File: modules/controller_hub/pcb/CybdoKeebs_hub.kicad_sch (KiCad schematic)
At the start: 5 parts, among them J1 USB_C_Receptacle_USB2.0_14P, U1 RP2040, U2 CH334F

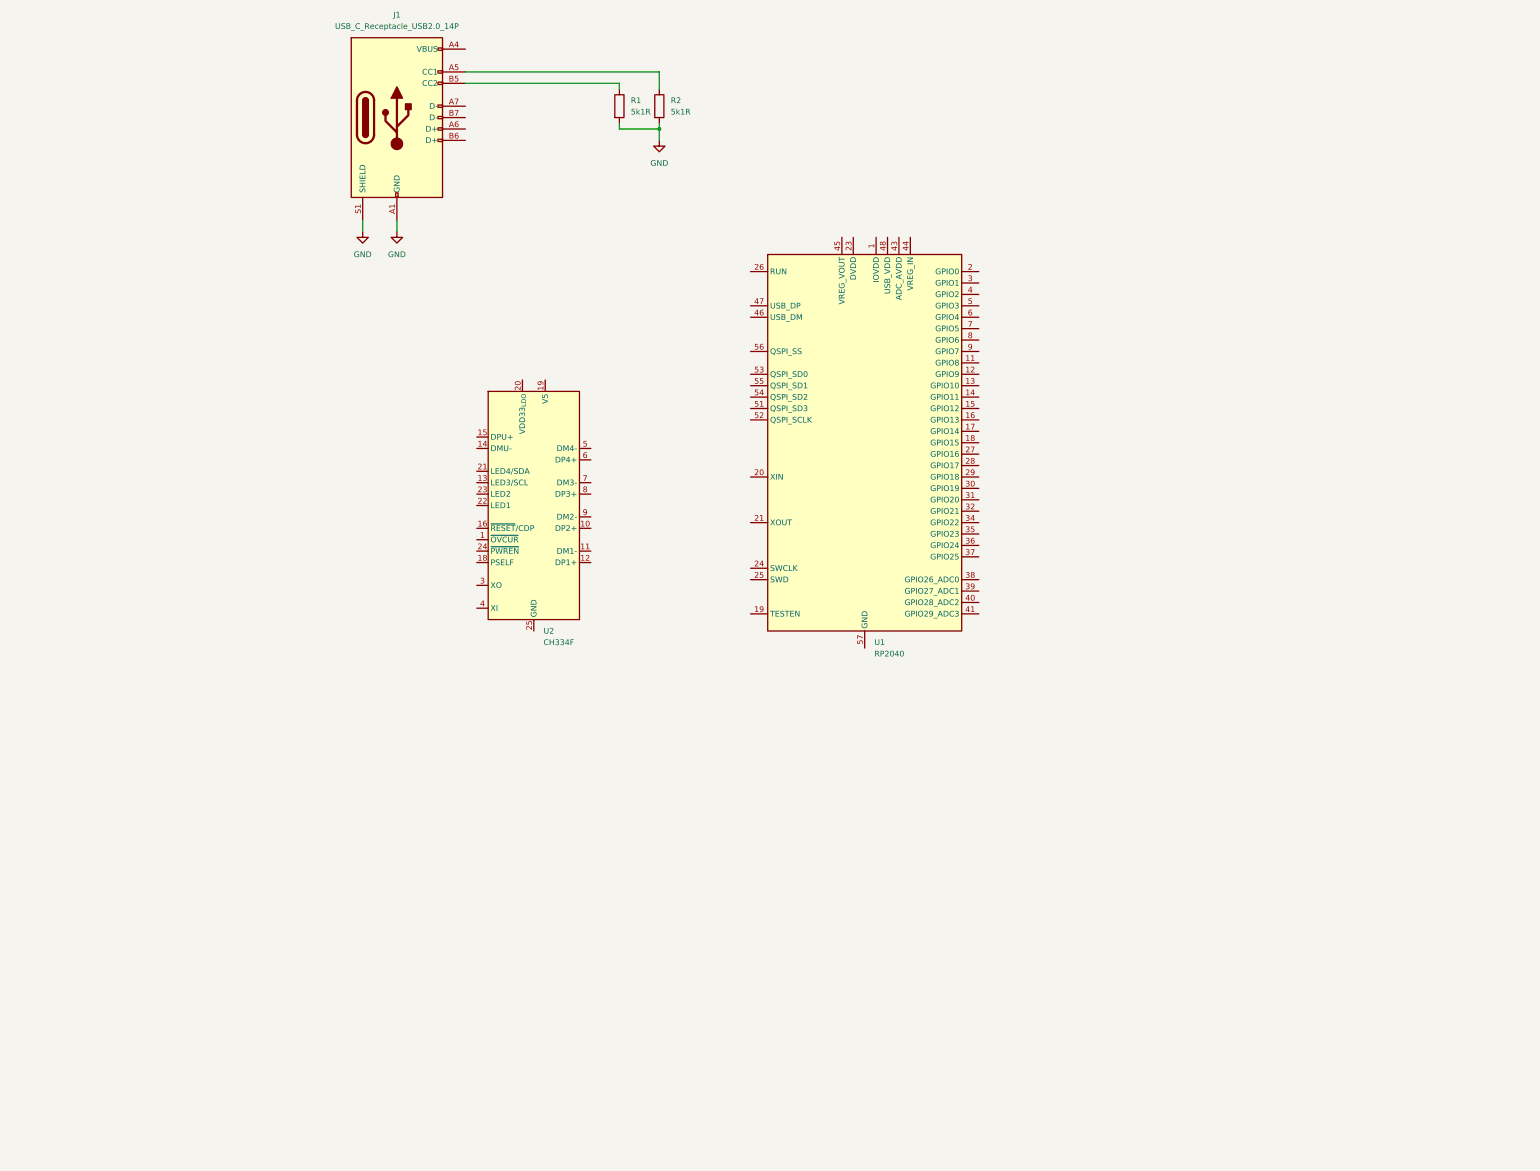
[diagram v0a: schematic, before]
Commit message: finish minimum system, add i2c connectors
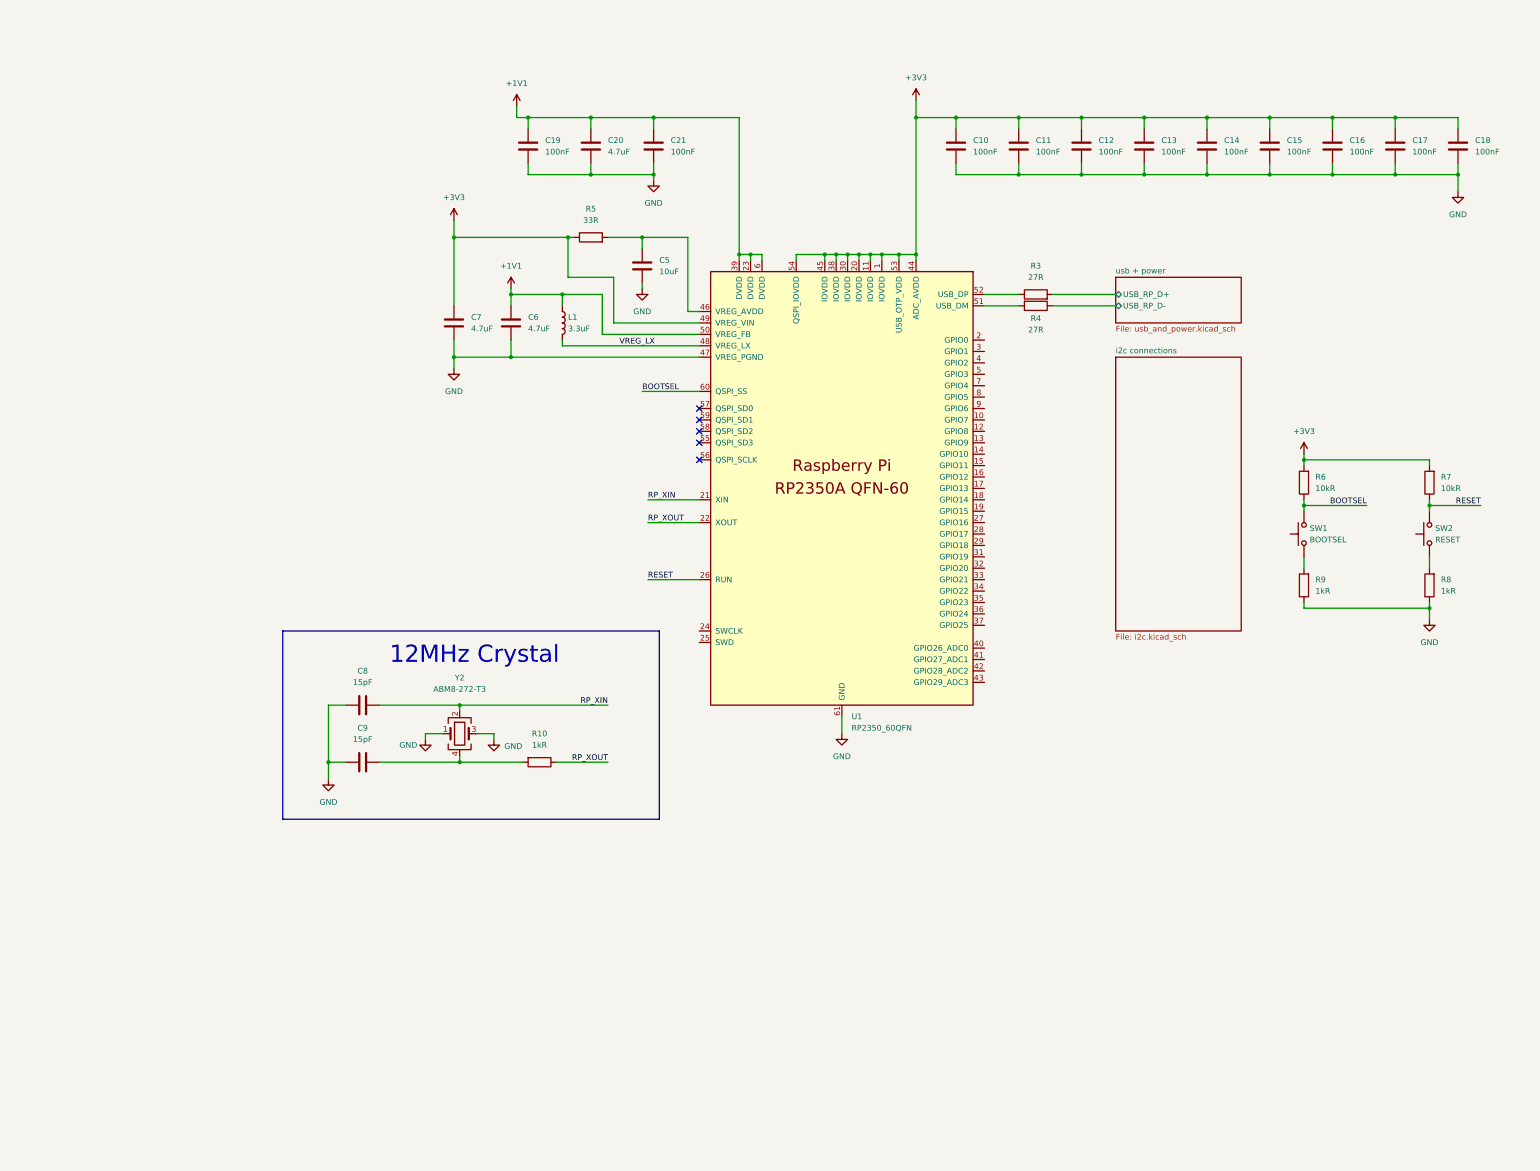
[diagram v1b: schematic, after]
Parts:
- removed J1: USB_C_Receptacle_USB2.0_14P, symbol Connector:USB_C_Receptacle_USB2.0_14P
- removed R1, R2: 5k1R, symbol Device:R
- removed U1: RP2040, Package_DFN_QFN:QFN-56-1EP_7x7mm_P0.4mm_EP3.2x3.2mm, symbol MCU_RaspberryPi:RP2040
- removed U2: CH334F, Package_DFN_QFN:QFN-24-1EP_4x4mm_P0.5mm_EP2.7x2.7mm, symbol Interface_USB:CH334F
- added C10, C11, C12, C13, C14, C15, C16, C17, C18, C19, C21: 100nF, Capacitor_SMD:C_0402_1005Metric_Pad0.74x0.62mm_HandSolder, symbol Device:C
- added C20, C6, C7: 4.7uF, Capacitor_SMD:C_0402_1005Metric_Pad0.74x0.62mm_HandSolder, symbol Device:C
- added C5: 10uF, Capacitor_SMD:C_0402_1005Metric_Pad0.74x0.62mm_HandSolder, symbol Device:C
- added C8, C9: 15pF, Capacitor_SMD:C_0402_1005Metric_Pad0.74x0.62mm_HandSolder, symbol Device:C
- added L1: 3.3uF, symbol Device:L
- added R10, R8, R9: 1kR, symbol Device:R
- added R3, R4: 27R, Resistor_SMD:R_0402_1005Metric_Pad0.72x0.64mm_HandSolder, symbol Device:R
- added R5: 33R, symbol Device:R
- added R6, R7: 10kR, symbol Device:R
- added SW1: BOOTSEL, symbol Switch:SW_Push
- added SW2: RESET, symbol Switch:SW_Push
- added U1: RP2350_60QFN, RP2350_60QFN_minimal:RP2350-QFN-60-1EP_7x7_P0.4mm_EP3.4x3.4mm_ThermalVias, symbol MCU_RaspberryPi_RP2350:RP2350_60QFN
- added Y2: ABM8-272-T3, symbol Device:Crystal_GND24
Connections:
- net GND: now also C10.2, C11.2, C12.2, C13.2, C14.2, C15.2, C16.2, C17.2, C18.2, C19.2, C20.2, C21.2, C5.2, C6.2, C7.2, C8.1, C9.1, R8.1, R9.1, U1.47 (VREG_PGND), U1.61 (GND), Y2.1, Y2.3
- new net: R9.2, SW1.1
- new net: R8.2, SW2.1
- new net: C5.1, R5.2, U1.46 (VREG_AVDD)
- new net: C9.2, R10.2, Y2.4
- new net: R3.1, U1.52 (USB_DP)
- new net: R4.2, U1.51 (USB_DM)
- new net +1V1: C19.1, C20.1, C21.1, C6.1, L1.1, U1.23 (DVDD), U1.39 (DVDD), U1.50 (VREG_FB), U1.6 (DVDD)
- new net +3V3: C10.1, C11.1, C12.1, C13.1, C14.1, C15.1, C16.1, C17.1, C18.1, C7.1, R5.1, R6.2, R7.2, U1.1 (IOVDD), U1.11 (IOVDD), U1.20 (IOVDD), U1.30 (IOVDD), U1.38 (IOVDD), U1.44 (ADC_AVDD), U1.45 (IOVDD), U1.49 (VREG_VIN), U1.53 (USB_OTP_VDD), U1.54 (QSPI_IOVDD)
- new net BOOTSEL: R6.1, SW1.2, U1.60 (QSPI_SS)
- new net RESET: R7.1, SW2.2, U1.26 (RUN)
- new net RP_XIN: C8.2, U1.21 (XIN), Y2.2
- new net RP_XOUT: R10.1, U1.22 (XOUT)
- new net VREG_LX: L1.2, U1.48 (VREG_LX)
- new net usb + power/USB_RP_D+: R3.2
- new net usb + power/USB_RP_D-: R4.1
- no-connect marks 0 -> 5
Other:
- added sheet i2c connections (i2c.kicad_sch)
- added sheet usb + power (usb_and_power.kicad_sch)
- note added: "12MHz Crystal"

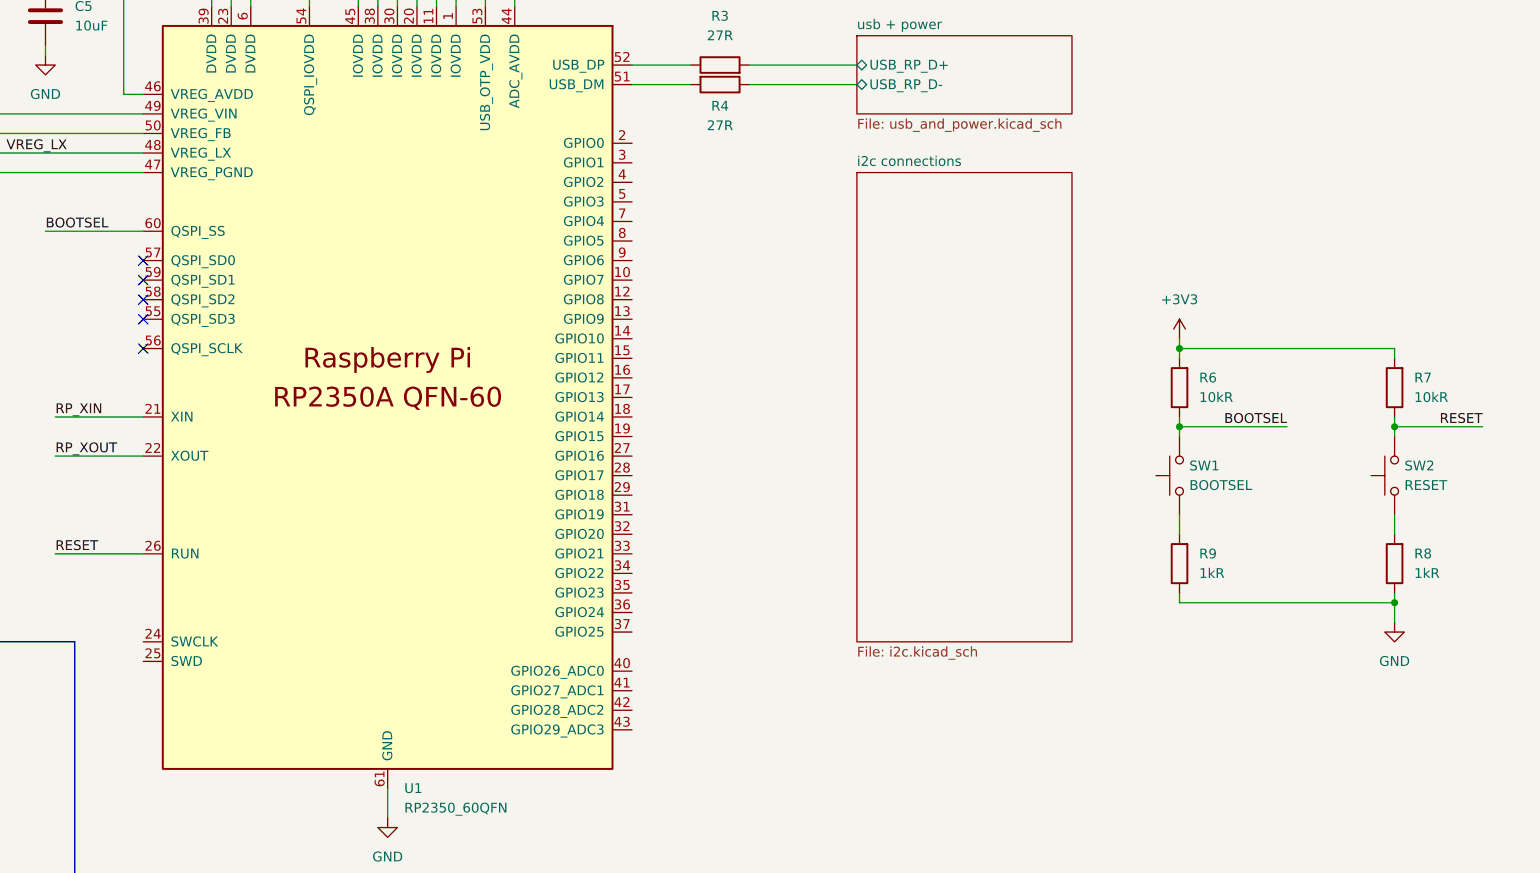
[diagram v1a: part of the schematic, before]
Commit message: add template for each module
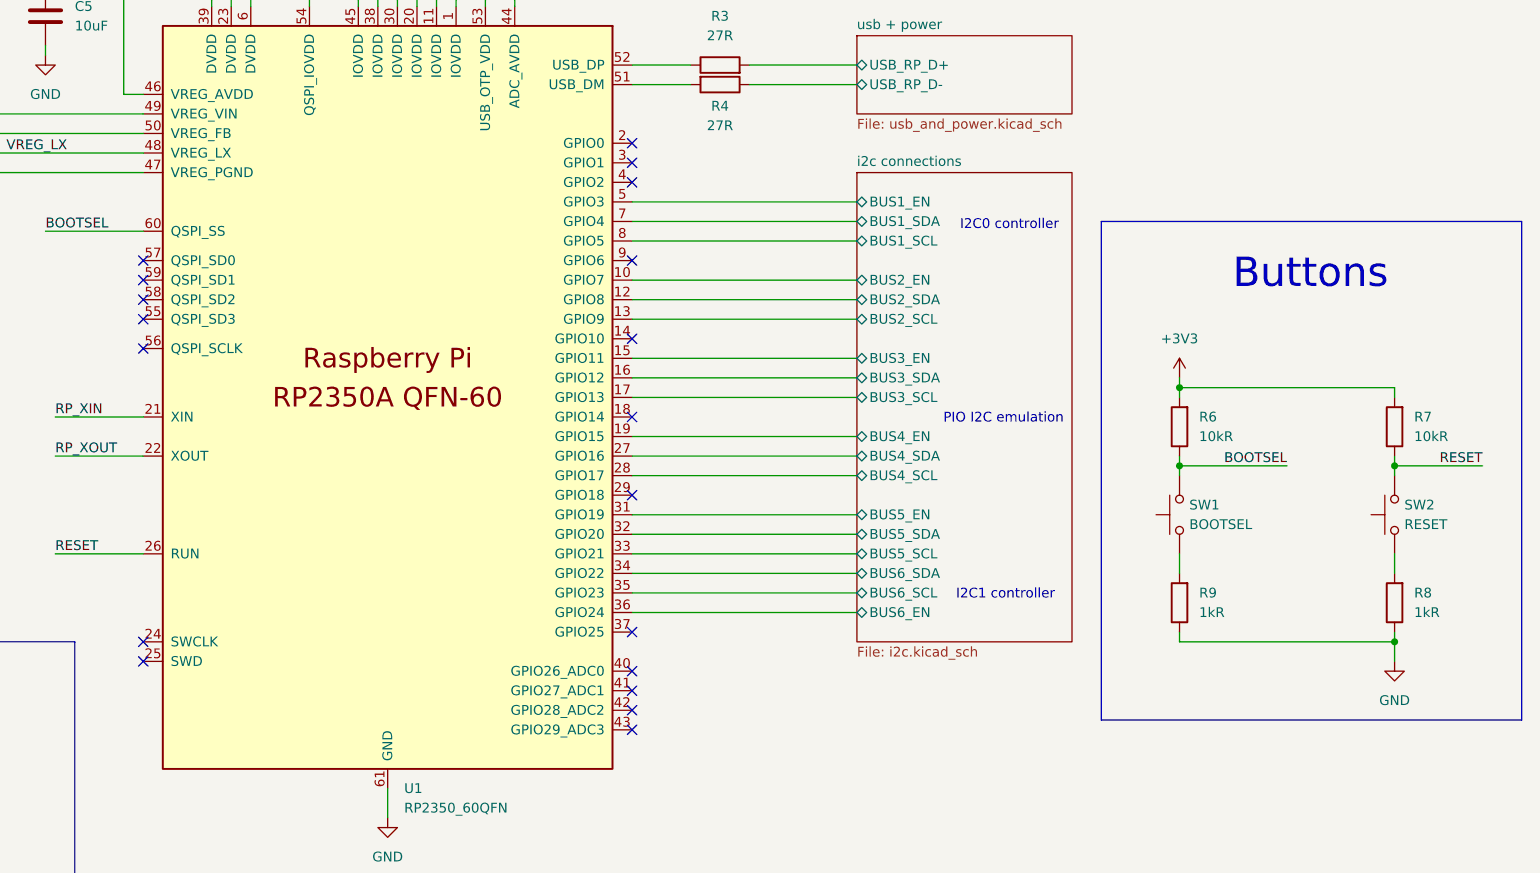
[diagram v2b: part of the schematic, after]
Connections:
- net i2c connections/BUS2_EN: now reaches U1.10 (GPIO7)
- net i2c connections/BUS2_SDA: now reaches U1.12 (GPIO8)
- net i2c connections/BUS2_SCL: now reaches U1.13 (GPIO9)
- net i2c connections/BUS3_EN: now reaches U1.15 (GPIO11)
- net i2c connections/BUS3_SDA: now reaches U1.16 (GPIO12)
- net i2c connections/BUS3_SCL: now reaches U1.17 (GPIO13)
- net i2c connections/BUS4_EN: now reaches U1.19 (GPIO15)
- net i2c connections/BUS4_SDA: now reaches U1.27 (GPIO16)
- net i2c connections/BUS4_SCL: now reaches U1.28 (GPIO17)
- net i2c connections/BUS5_EN: now reaches U1.31 (GPIO19)
- net i2c connections/BUS5_SDA: now reaches U1.32 (GPIO20)
- net i2c connections/BUS5_SCL: now reaches U1.33 (GPIO21)
- net i2c connections/BUS6_SDA: now reaches U1.34 (GPIO22)
- net i2c connections/BUS6_SCL: now reaches U1.35 (GPIO23)
- net i2c connections/BUS6_EN: now reaches U1.36 (GPIO24)
- net i2c connections/BUS1_EN: now reaches U1.5 (GPIO3)
- net i2c connections/BUS1_SDA: now reaches U1.7 (GPIO4)
- net i2c connections/BUS1_SCL: now reaches U1.8 (GPIO5)
- no-connect marks 5 -> 19
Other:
- sheet i2c connections ports: added BUS1_EN, BUS1_SCL, BUS1_SDA, BUS2_EN, BUS2_SCL, BUS2_SDA, BUS3_EN, BUS3_SCL, BUS3_SDA, BUS4_EN, BUS4_SCL, BUS4_SDA, BUS5_EN, BUS5_SCL, BUS5_SDA, BUS6_EN, BUS6_SCL, BUS6_SDA; removed none
- note added: "Buttons"
- note added: "I2C0 controller"
- note added: "I2C1 controller"
- note added: "PIO I2C emulation"
- moved on the sheet: R6, R7, R8, R9, SW1, SW2

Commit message: hub done, started macropad
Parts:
- removed C10, C11, C12: 100nF, Capacitor_SMD:C_0402_1005Metric_Pad0.74x0.62mm_HandSolder, symbol Device:C
- added H1, H2, H3: MountingHole, MountingHole:MountingHole_3.2mm_M3, symbol Mechanical:MountingHole
- L1: footprint (none) -> imports:INDC1608X95N
- R1: renamed from R10; footprint (none) -> Resistor_SMD:R_0402_1005Metric_Pad0.72x0.64mm_HandSolder
- R2: renamed from R5; footprint (none) -> Resistor_SMD:R_0402_1005Metric_Pad0.72x0.64mm_HandSolder
- R5: renamed from R6; footprint (none) -> Resistor_SMD:R_0402_1005Metric_Pad0.72x0.64mm_HandSolder
- R6: renamed from R9; footprint (none) -> Resistor_SMD:R_0402_1005Metric_Pad0.72x0.64mm_HandSolder
- R7, R8: footprint (none) -> Resistor_SMD:R_0402_1005Metric_Pad0.72x0.64mm_HandSolder
- SW1, SW2: footprint (none) -> Button_Switch_SMD:SW_Push_SPST_NO_Alps_SKRK
- Y1: renamed from Y2; footprint (none) -> Crystal:Crystal_SMD_Abracon_ABM8G-4Pin_3.2x2.5mm
- renumbered C8 to C1, C14 to C10, C15 to C11, C16 to C12, C17 to C13, C18 to C14, C9 to C2, C7 to C3, C6 to C4, C19 to C5, C20 to C6, C5 to C7, C21 to C8, C13 to C9
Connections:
- net GND: now also Y1.2, Y1.4; no longer Y1.1, Y1.3
- net RP_XIN: now also Y1.1; no longer Y1.2
- net i2c connections/BUS4_EN: now also U1.27 (GPIO16); no longer U1.19 (GPIO15)
- net i2c connections/BUS4_SCL: now also U1.29 (GPIO18); no longer U1.28 (GPIO17)
- net i2c connections/BUS4_SDA: now also U1.28 (GPIO17); no longer U1.27 (GPIO16)
- net i2c connections/BUS6_EN: now also U1.34 (GPIO22); no longer U1.36 (GPIO24)
- net i2c connections/BUS6_SCL: now also U1.36 (GPIO24); no longer U1.35 (GPIO23)
- net i2c connections/BUS6_SDA: now also U1.35 (GPIO23); no longer U1.34 (GPIO22)
- net at C2.2, R1.2: now also Y1.3; no longer Y1.4
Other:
- moved on the sheet: C10, C11, C12, C13, C14, C9, Y1

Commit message: finished all pcbs
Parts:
- added R11, R12, R13, R14, R15, R16, R17, R18, R19, R20, R21, R22: 10kR, Resistor_SMD:R_0402_1005Metric_Pad0.72x0.64mm_HandSolder, symbol Device:R
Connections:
- net +3V3: now also R11.2, R12.2, R13.2, R14.2, R15.2, R16.2, R17.2, R18.2, R19.2, R20.2, R21.2, R22.2
- net GND: no longer C10.2, C11.2, C12.2, C13.2
- net i2c connections/BUS1_SCL: now also R21.1
- net i2c connections/BUS1_SDA: now also R22.1
- net i2c connections/BUS2_SCL: now also R19.1
- net i2c connections/BUS2_SDA: now also R20.1
- net i2c connections/BUS3_SCL: now also R17.1
- net i2c connections/BUS3_SDA: now also R18.1
- net i2c connections/BUS4_SCL: now also R15.1
- net i2c connections/BUS4_SDA: now also R16.1
- net i2c connections/BUS5_SCL: now also R13.1
- net i2c connections/BUS5_SDA: now also R14.1
- net i2c connections/BUS6_SCL: now also R11.1
- net i2c connections/BUS6_SDA: now also R12.1
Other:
- moved on the sheet: C10, C11, C12, C13, C14, C9, R3, R4, R5, R6, R7, R8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

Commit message: ship ship ship!!!
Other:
- moved on the sheet: R5, R6, R7, R8, SW1, SW2
